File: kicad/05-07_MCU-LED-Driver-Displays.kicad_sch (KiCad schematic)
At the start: 63 parts, among them J6 Conn_02x08_Counter_Clockwise, J7 Conn_01x03_Pin, J8 Conn_01x03_Pin, Q4 AO3400A, Q5 AO3400A, Q7 AO3400A, Q8 AO3400A, SW1 B3U-1100PM, SW2 BOOTSEL, SW3 RESET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

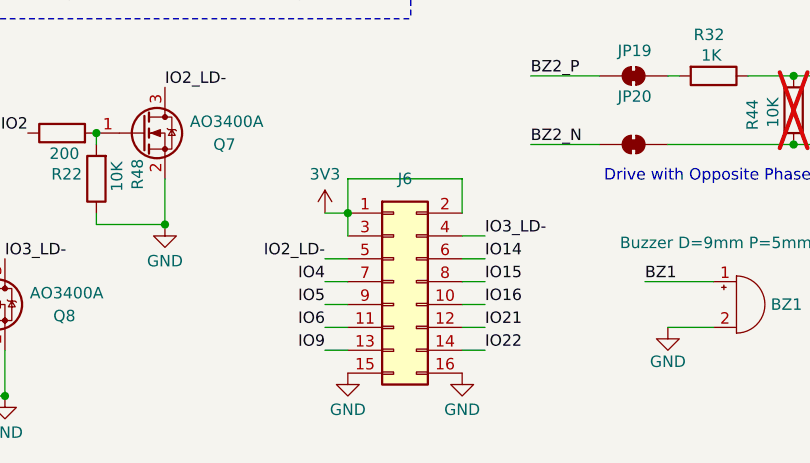
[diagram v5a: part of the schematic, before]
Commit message: routing - GPIOs
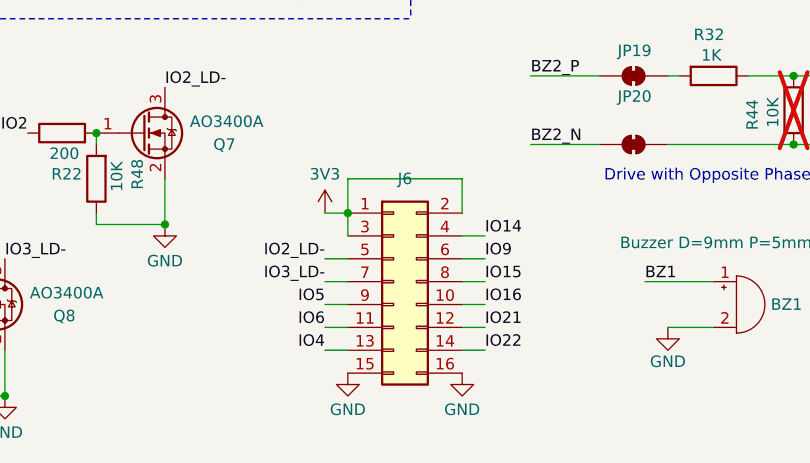
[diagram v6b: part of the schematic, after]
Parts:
- J6: footprint Connector_PinHeader_2.54mm:PinHeader_2x07_P2.54mm_Vertical -> Connector_PinHeader_2.54mm:PinHeader_2x08_P2.54mm_Vertical
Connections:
- net IO14: now also J6.4 (Pin_4); no longer J6.6 (Pin_6)
- net IO3_LD-: now also J6.7 (Pin_7); no longer J6.4 (Pin_4)
- net IO4: now also J6.13 (Pin_13); no longer J6.7 (Pin_7)
- net IO9: now also J6.6 (Pin_6); no longer J6.13 (Pin_13)
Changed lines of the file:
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@@
-		)
-	)
-	(label "IO4"
-		(at 67.31 180.34 180)
-		(effects
-			(font
-				(size 1.27 1.27)
-			)
-			(justify right bottom)
 		)
 	)
@@
 		)
 	)
+	(label "IO3_LD-"
+		(at 67.31 180.34 180)
+		(effects
+			(font
+				(size 1.27 1.27)
+			)
+			(justify right bottom)
+		)
+	)
 	(label "IO21"
 		(at 179.07 110.49 180)
@@
 		)
 	)
+	(label "IO4"
+		(at 67.31 187.96 180)
+		(effects
+			(font
+				(size 1.27 1.27)
+			)
+			(justify right bottom)
+		)
+	)
 	(label "IO2_LD-"
 		(at 67.31 177.8 180)
@@
 		)
 	)
-	(label "IO14"
-		(at 85.09 177.8 0)
-		(effects
-			(font
-				(size 1.27 1.27)
-			)
-			(justify left bottom)
-		)
-	)
 	(label "IO16"
 		(at 85.09 182.88 0)
@@
 	)
 	(label "IO9"
+		(at 85.09 177.8 0)
+		(effects
+			(font
+				(size 1.27 1.27)
+			)
+			(justify left bottom)
+		)
+	)
+	(label "IO14"
+		(at 85.09 175.26 0)
+		(effects
+			(font
+				(size 1.27 1.27)
+			)
+			(justify left bottom)
+		)
+	)
+	(label "IO9"
 		(at 179.07 80.01 180)
-		(effects
-			(font
-				(size 1.27 1.27)
-			)
-			(justify right bottom)
-		)
-	)
-	(label "IO9"
-		(at 67.31 187.96 180)
 		(effects
 			(font
@@
 			)
 			(justify right bottom)
-		)
-	)
-	(label "IO3_LD-"
-		(at 85.09 175.26 0)
-		(effects
-			(font
-				(size 1.27 1.27)
-			)
-			(justify left bottom)
 		)
 	)
@@
 			)
 		)
-		(property "Footprint" "Connector_PinHeader_2.54mm:PinHeader_2x07_P2.54mm_Vertical"
+		(property "Footprint" "Connector_PinHeader_2.54mm:PinHeader_2x08_P2.54mm_Vertical"
 			(at 74.93 180.34 0)
 			(effects

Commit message: production files for PCBWay initial - BOM manually edited for PCBA
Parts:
- BZ1, J6, J7, J8: now not fitted
- R44: now fitted
- SW2, SW3, SW4, SW5: MPN (Generic) -> (Generic)/1825910-6; Manufacturer (Generic) -> (Generic)/TE; Supplier 1 (Generic) -> (Generic)/Digikey; Supplier 1 URL (none) -> https://www.digikey.jp/en/products/detail/te-connectivity-a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; now not fitted
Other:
- moved on the sheet: SW1
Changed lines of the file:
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@@
 		(in_bom yes)
 		(on_board yes)
-		(dnp yes)
+		(dnp no)
 		(property "Reference" "R44"
 			(at 114.808 161.798 90)
@@
 		(in_bom yes)
 		(on_board yes)
-		(dnp no)
+		(dnp yes)
 		(property "Reference" "J7"
 			(at 196.342 59.69 0)
@@
 		(in_bom yes)
 		(on_board yes)
-		(dnp no)
+		(dnp yes)
 		(fields_autoplaced yes)
 		(property "Reference" "J6"
@@
 		(in_bom yes)
 		(on_board yes)
-		(dnp no)
+		(dnp yes)
 		(fields_autoplaced yes)
 		(property "Reference" "SW3"
@@
 			)
 		)
-		(property "MPN" "(Generic)"
+		(property "MPN" "(Generic)/1825910-6"
 			(at 100.33 57.15 0)
 			(effects
@@
 			)
 		)
-		(property "Manufacturer" "(Generic)"
+		(property "Manufacturer" "(Generic)/TE"
 			(at 100.33 57.15 0)
 			(effects
@@
 			)
 		)
-		(property "Supplier 1" "(Generic)"
+		(property "Supplier 1" "(Generic)/Digikey"
 			(at 100.33 57.15 0)
 			(effects
@@
 			)
 		)
+		(property "Supplier 1 URL" "https://www.digikey.jp/en/products/detail/te-connectivity-alcoswitch-switches/1825910-6/1632536?_gl=1*h967is*_up*MQ..*_gs*MQ..&gclsrc=aw.ds"
+			(at 100.33 57.15 0)
+			(effects
+				(font
+					(size 1.27 1.27)
+				)
+				(hide yes)
+			)
+		)
 		(pin "1"
 		)
@@
 		(in_bom yes)
 		(on_board yes)
-		(dnp no)
+		(dnp yes)
 		(fields_autoplaced yes)
 		(property "Reference" "SW5"
@@
 			)
 		)
-		(property "MPN" "(Generic)"
+		(property "MPN" "(Generic)/1825910-6"
 			(at 241.3 114.3 0)
 			(effects
@@
 			)
 		)
-		(property "Manufacturer" "(Generic)"
+		(property "Manufacturer" "(Generic)/TE"
 			(at 241.3 114.3 0)
 			(effects
@@
 			)
 		)
-		(property "Supplier 1" "(Generic)"
+		(property "Supplier 1" "(Generic)/Digikey"
 			(at 241.3 114.3 0)
 			(effects
@@
 			)
 		)
+		(property "Supplier 1 URL" "https://www.digikey.jp/en/products/detail/te-connectivity-alcoswitch-switches/1825910-6/1632536?_gl=1*h967is*_up*MQ..*_gs*MQ..&gclsrc=aw.ds"
+			(at 241.3 114.3 0)
+			(effects
+				(font
+					(size 1.27 1.27)
+				)
+				(hide yes)
+			)
+		)
 		(pin "1"
 		)
@@
 	(symbol
 		(lib_id "Switch:SW_Push")
-		(at 13.97 -11.43 0)
+		(at 22.86 218.44 0)
 		(unit 1)
 		(exclude_from_sim no)
@@
 		(fields_autoplaced yes)
 		(property "Reference" "SW1"
-			(at 13.97 -19.05 0)
+			(at 22.86 210.82 0)
 			(effects
 				(font
@@
 		)
 		(property "Value" "B3U-1100PM"
-			(at 13.97 -16.51 0)
+			(at 22.86 213.36 0)
 			(effects
 				(font
@@
 		)
 		(property "Footprint" "Button_Switch_SMD:SW_SPST_B3U-1100P"
-			(at 13.97 -16.51 0)
+			(at 22.86 213.36 0)
 			(effects
 				(font
@@
 		)
 		(property "Datasheet" "~"
-			(at 13.97 -16.51 0)
+			(at 22.86 213.36 0)
 			(effects
 				(font
@@
 		)
 		(property "Description" "SWITCH TACTILE SPST-NO 0.05A 12V"
-			(at 13.97 -11.43 0)
+			(at 22.86 218.44 0)
 			(effects
 				(font
@@
 		)
 		(property "Subsystem" "05-MCU-XTAL-FLASH"
-			(at 13.97 -11.43 0)
+			(at 22.86 218.44 0)
 			(effects
 				(font
@@
 		)
 		(property "MPN" "B3U-1100PM"
-			(at 13.97 -11.43 0)
+			(at 22.86 218.44 0)
 			(effects
 				(font
@@
 		)
 		(property "Manufacturer" "omron"
-			(at 13.97 -11.43 0)
+			(at 22.86 218.44 0)
 			(effects
 				(font
@@
 		)
 		(property "Package" "SMD 4mmx2.5mm"
-			(at 13.97 -11.43 0)
+			(at 22.86 218.44 0)
 			(effects
 				(font
@@
 		)
 		(property "Supplier 1" "Digikey"
-			(at 13.97 -11.43 0)
+			(at 22.86 218.44 0)
 			(effects
 				(font
@@
 		)
 		(property "Supplier 1 URL" "https://www.digikey.jp/en/products/detail/omron-electronics-inc-emc-div/B3U-1100PM/3908607?gclsrc=aw.ds&gad_source=1&gad_campaignid=20220851003"
-			(at 13.97 -11.43 0)
+			(at 22.86 218.44 0)
 			(effects
 				(font
@@
 		)
 		(property "Lab_In_Stock" "Y"
-			(at 13.97 -11.43 0)
+			(at 22.86 218.44 0)
 			(effects
 				(font
@@
 		(in_bom yes)
 		(on_board yes)
-		(dnp no)
+		(dnp yes)
 		(property "Reference" "BZ1"
 			(at 116.84 182.88 0)
@@
 		(in_bom yes)
 		(on_board yes)
-		(dnp no)
+		(dnp yes)
 		(property "Reference" "J8"
 			(at 199.39 132.0799 0)
@@
 		(in_bom yes)
 		(on_board yes)
-		(dnp no)
+		(dnp yes)
 		(fields_autoplaced yes)
 		(property "Reference" "SW4"
@@
 			)
 		)
-		(property "MPN" "(Generic)"
+		(property "MPN" "(Generic)/1825910-6"
 			(at 240.03 82.55 0)
 			(effects
@@
 			)
 		)
-		(property "Manufacturer" "(Generic)"
+		(property "Manufacturer" "(Generic)/TE"
 			(at 240.03 82.55 0)
 			(effects
@@
 			)
 		)
-		(property "Supplier 1" "(Generic)"
+		(property "Supplier 1" "(Generic)/Digikey"
 			(at 240.03 82.55 0)
 			(effects
@@
 			)
 		)
+		(property "Supplier 1 URL" "https://www.digikey.jp/en/products/detail/te-connectivity-alcoswitch-switches/1825910-6/1632536?_gl=1*h967is*_up*MQ..*_gs*MQ..&gclsrc=aw.ds"
+			(at 240.03 82.55 0)
+			(effects
+				(font
+					(size 1.27 1.27)
+				)
+				(hide yes)
+			)
+		)
 		(pin "1"
 		)
@@
 		(in_bom yes)
 		(on_board yes)
-		(dnp no)
+		(dnp yes)
 		(fields_autoplaced yes)
 		(property "Reference" "SW2"
@@
 			)
 		)
-		(property "MPN" "(Generic)"
+		(property "MPN" "(Generic)/1825910-6"
 			(at 50.8 60.96 0)
 			(effects
@@
 			)
 		)
-		(property "Manufacturer" "(Generic)"
+		(property "Manufacturer" "(Generic)/TE"
 			(at 50.8 60.96 0)
 			(effects
@@
 			)
 		)
-		(property "Supplier 1" "(Generic)"
+		(property "Supplier 1" "(Generic)/Digikey"
 			(at 50.8 60.96 0)
 			(effects
@@
 			)
 		)
-		(property "Supplier 1 URL" ""
+		(property "Supplier 1 URL" "https://www.digikey.jp/en/products/detail/te-connectivity-alcoswitch-switches/1825910-6/1632536?_gl=1*h967is*_up*MQ..*_gs*MQ..&gclsrc=aw.ds"
 			(at 50.8 60.96 0)
 			(effects

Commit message: fabrication files, after edits for pcbway 2-12
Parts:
- R33: value 1 -> 0
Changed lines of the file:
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@@
 			)
 		)
-		(property "Value" "1"
+		(property "Value" "0"
 			(at 159.512 34.544 90)
 			(effects
